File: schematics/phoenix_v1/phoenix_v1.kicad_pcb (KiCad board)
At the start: 2 copper layers, 106 x 64.5 mm, 15 parts, among them J1 Screw_Terminal_01x02, J2 Conn_01x09_Socket, SW1 RotaryEncoder_Switch, U2 ESP32-S3-DevKitC, U3 NHD-C0220BIZ

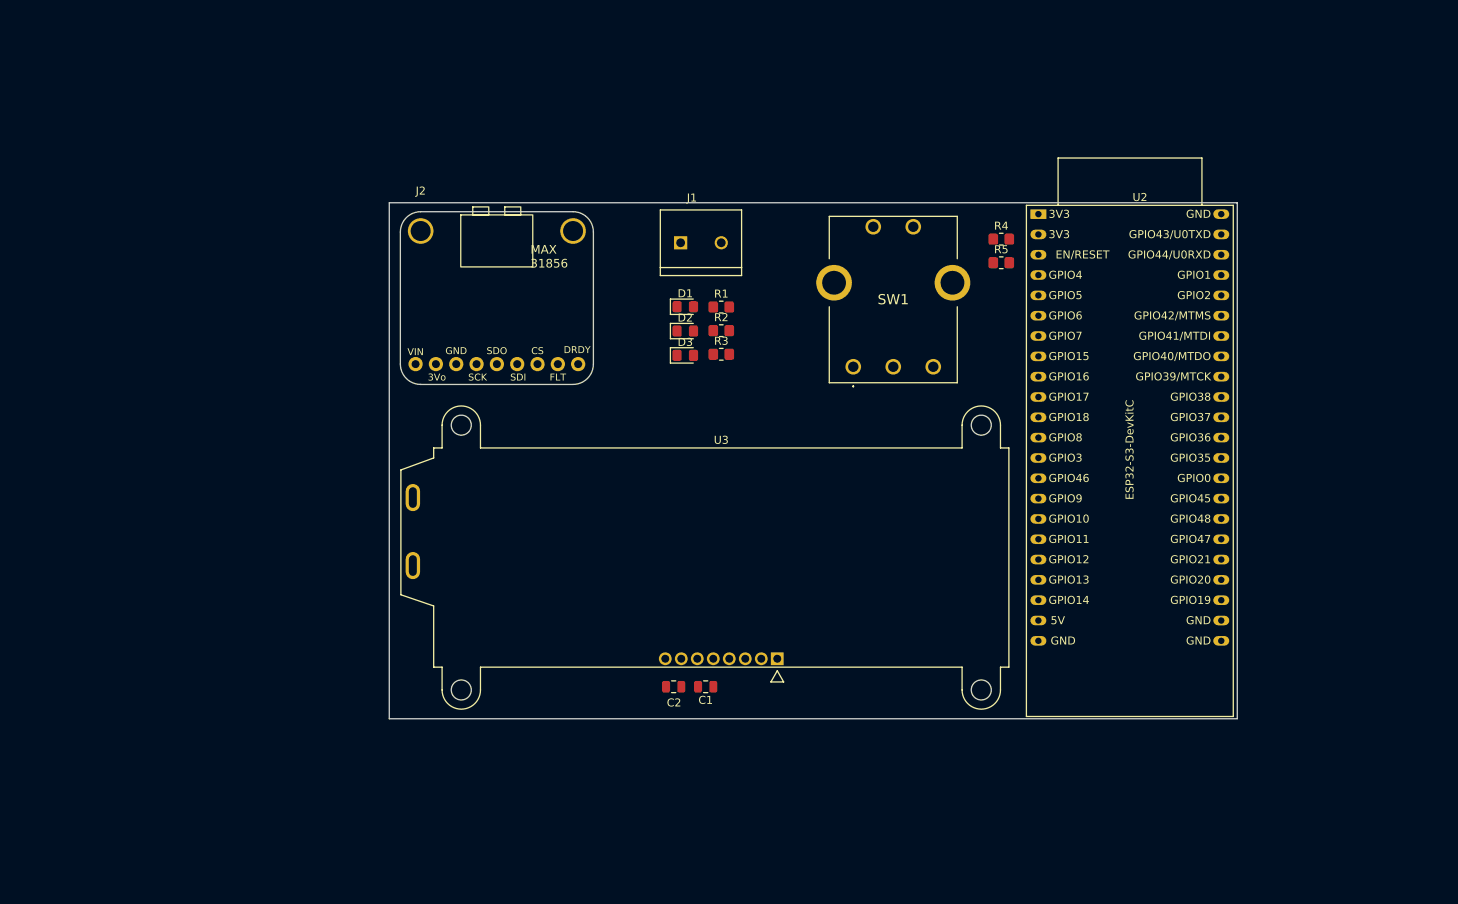
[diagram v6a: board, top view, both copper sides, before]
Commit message: routing (#28)
* make board outline silkscreen instead of edgecuts

* some wiring

* update pcb for max footprint

* cleanup max header

* route everything and GND fill and via stitch

* title blocks

* export pdfs

* fix "Dont mix global and local net labels for the same net (SSR_PWM)"

* fix "it should be made clear on the schematic that U1 and surrounding components are off board"

* fix "NHD-CO22BIZ needs 3.3V not 5V"

* connect A and K on lcd

* fix "routing for the I2C pullups VDD trace"

* fix "more space on display mounting holes"

* upload DRU

* fix new DRC errors

* more vias

* zip gerber script

* generate GERB

* update zip script for new path

* zip

* HF log!!!!!!!!

* add logo in

* hf logo as footprint

* update gerb

* add names and mounting holes

* fix J1 missing

* zip

---------

Co-authored-by: Waterloo Hacker Fab <waterloofab@hackerfabmacmini.uwaterloo.ca>
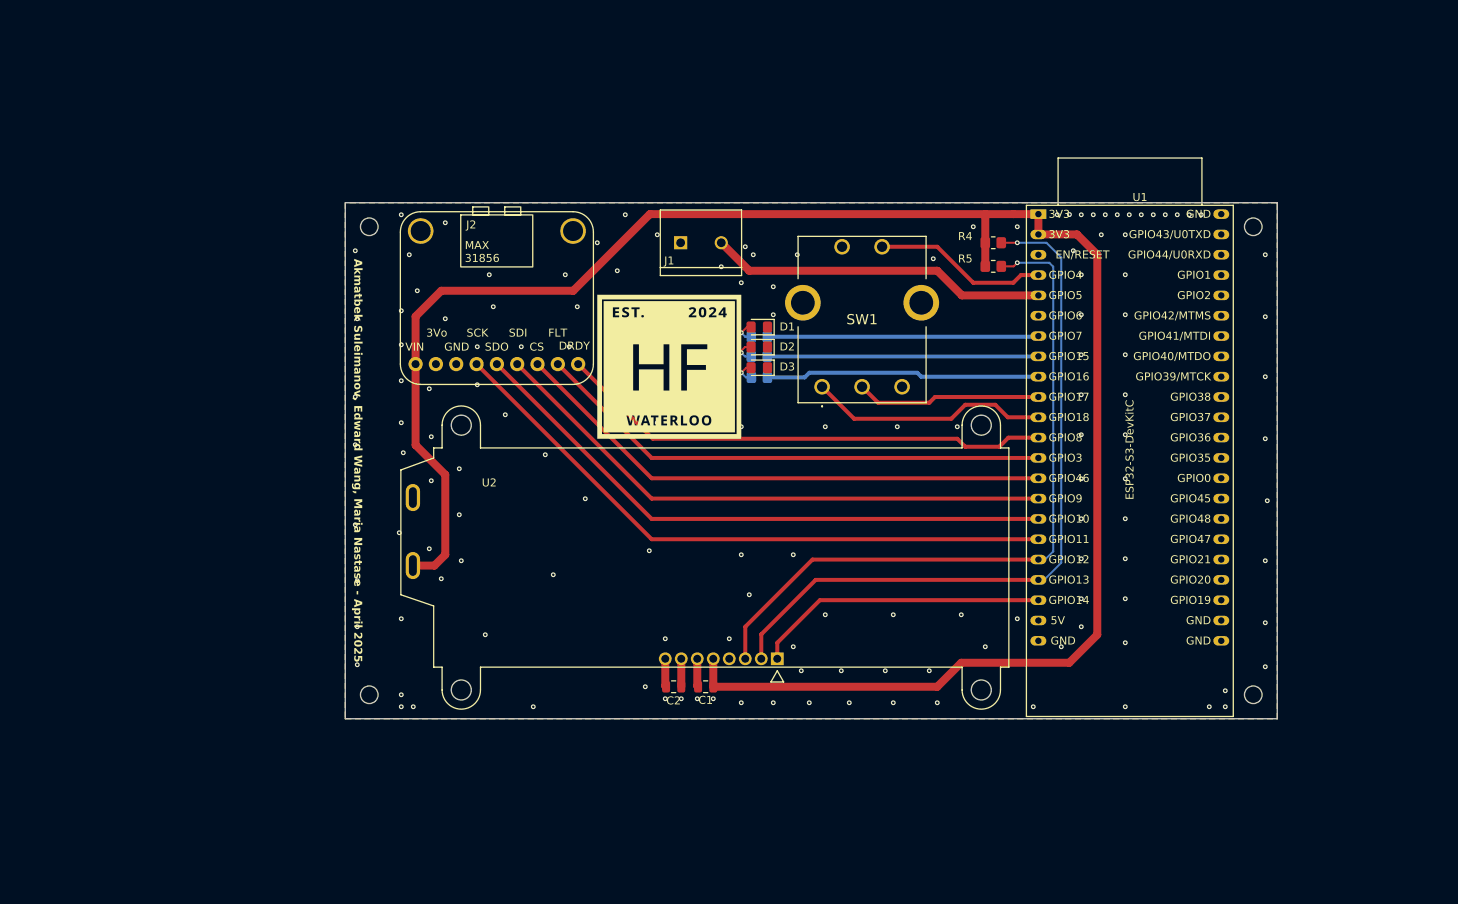
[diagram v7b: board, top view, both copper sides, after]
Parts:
- added G***: LOGO, !footprints:HF_logo, F.Cu at (119.0, 79.0)
- added REF**: MountingHole_2.2mm_M2, MountingHole:MountingHole_2.2mm_M2, F.Cu at (192.0, 120.0)
- added REF**: MountingHole_2.2mm_M2, MountingHole:MountingHole_2.2mm_M2, F.Cu at (81.5, 61.5)
- added REF**: MountingHole_2.2mm_M2, MountingHole:MountingHole_2.2mm_M2, F.Cu at (81.5, 120.0)
- added REF**: MountingHole_2.2mm_M2, MountingHole:MountingHole_2.2mm_M2, F.Cu at (192.0, 61.5)
- R1, R2, R3: moved to B.Cu
- moved D1 9.59 mm to (130.2, 74.0), turned to 180 degrees
- moved D2 9.46 mm to (130.2, 76.5), turned to 180 degrees
- moved D3 9.38 mm to (130.2, 79.1), turned to 180 degrees
- moved R1 6.03 mm to (130.2, 75.2), turned to 180 degrees
- moved R2 5.74 mm to (130.2, 77.7), turned to 180 degrees
- moved R3 5.57 mm to (130.3, 80.3), turned to 180 degrees
- moved SW1 4.63 mm to (138.1, 81.5)
- moved R4 1.10 mm to (159.5, 63.5)
- moved R5 1.10 mm to (159.5, 66.5)
- renumbered U2 to U1, U3 to U2
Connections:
- C1 pad 1: +5V -> +3.3V
- J1 pad 2: SSR_PWM -> /SSR_PWM
- J2 pad 1: /DRDY -> /MAX_DRDY
- J2 pad 2: /~{FAULT} -> /MAX_FAULT
- J2 pad 3: /~{CS} -> /MAX_CS
- J2 pad 4: /SDI -> /MAX_SDI
- J2 pad 5: /SDO -> /MAX_SDO
- J2 pad 6: /SCK -> /MAX_SCK
- J2 pad 8: +3.3V -> /MAX_3.3VOUT
- J2 pad 9: /VIN_1 -> +3.3V
- R1 pad 1: Net-(U2-GPIO46) -> /LED_1
- R2 pad 1: Net-(U2-GPIO47) -> /LED_2
- R3 pad 1: Net-(U2-GPIO48) -> /LED_3
- U1 pad 10: unconnected-(U2-GPIO17/ADC2_CH6-Pad10) -> /ENC_B
- U1 pad 11: unconnected-(U2-GPIO18/ADC2_CH7-Pad11) -> /ENC_A
- U1 pad 12: unconnected-(U2-GPIO8/ADC1_CH7-Pad12) -> /MAX_DRDY
- U1 pad 13: unconnected-(U2-GPIO3/ADC1_CH2-Pad13) -> /MAX_FAULT
- U1 pad 14: Net-(U2-GPIO46) -> /MAX_CS
- U1 pad 15: unconnected-(U2-GPIO9/ADC1_CH8-Pad15) -> /MAX_SDI
- U1 pad 16: unconnected-(U2-GPIO10/ADC1_CH9-Pad16) -> /MAX_SDO
- U1 pad 17: unconnected-(U2-GPIO11/ADC2_CH0-Pad17) -> /MAX_SCK
- U1 pad 18: unconnected-(U2-GPIO12/ADC2_CH1-Pad18) -> /SDA
- U1 pad 19: unconnected-(U2-GPIO13/ADC2_CH2-Pad19) -> /SCL
- U1 pad 20: unconnected-(U2-GPIO14/ADC2_CH3-Pad20) -> /DISPLAY_RST
- U1 pad 27: SSR_PWM -> unconnected-(U1-GPIO21-Pad27)
- U1 pad 28: Net-(U2-GPIO47) -> unconnected-(U1-GPIO47-Pad28)
- U1 pad 29: Net-(U2-GPIO48) -> unconnected-(U1-GPIO48-Pad29)
- U1 pad 32: /DISPLAY_~{RST} -> unconnected-(U1-GPIO35-Pad32)
- U1 pad 33: /ENC_A -> unconnected-(U1-GPIO36-Pad33)
- U1 pad 34: /ENC_B -> unconnected-(U1-GPIO37-Pad34)
- U1 pad 35: /ENC_SW -> unconnected-(U1-GPIO38-Pad35)
- U1 pad 4: /SDA -> /ENC_SW
- U1 pad 5: /SCL -> /SSR_PWM
- U1 pad 7: unconnected-(U2-GPIO7/ADC1_CH6-Pad7) -> /LED_1
- U1 pad 8: unconnected-(U2-GPIO15/ADC2_CH4/32K_P-Pad8) -> /LED_2
- U1 pad 9: unconnected-(U2-GPIO16/ADC2_CH5/32K_N-Pad9) -> /LED_3
- U2 pad 1: /DISPLAY_~{RST} -> /DISPLAY_RST
- U2 pad 10: unconnected-(U3-K-Pad10) -> GND
- U2 pad 5: +5V -> +3.3V
- U2 pad 9: unconnected-(U3-A-Pad9) -> +3.3V
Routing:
- net +3.3V: track 0.00 -> 238.3 mm
- net /SCL: track 0.00 -> 90.7 mm, vias 0 -> 1
- net /SDA: track 0.00 -> 88.9 mm, vias 0 -> 1
- net /MAX_SCK: track 0.00 -> 79.3 mm
- net /MAX_SDO: track 0.00 -> 75.7 mm
- net /MAX_SDI: track 0.00 -> 72.1 mm
- net /MAX_CS: track 0.00 -> 68.5 mm
- net /MAX_FAULT: track 0.00 -> 64.9 mm
- net /MAX_DRDY: track 0.00 -> 62.3 mm
- net /SSR_PWM: track 0.00 -> 42.4 mm
- net /DISPLAY_RST: track 0.00 -> 36.8 mm
- net /LED_3: track 0.00 -> 34.3 mm
- net /LED_1: track 0.00 -> 33.9 mm
- net /LED_2: track 0.00 -> 33.9 mm
- net /ENC_A: track 0.00 -> 30.1 mm
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- added copper zone on B.Cu, net GND
- added copper zone on F.Cu, net GND
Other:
- board size 106 x 64.5 mm -> 116.5 x 64.5 mm
- board text added: "Akmatbek Suleimanov, Edward Wang, Maria Nastase - April 2025"
- board text added: "D1"
- board text added: "D2"
- board text added: "D3"
- board text added: "JLCJLCJLCJLC"
- board text added: "R1"
